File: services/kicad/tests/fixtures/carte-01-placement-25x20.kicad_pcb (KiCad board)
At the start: 2 copper layers, 24.8 x 17 mm, 5 parts, among them J1 IN

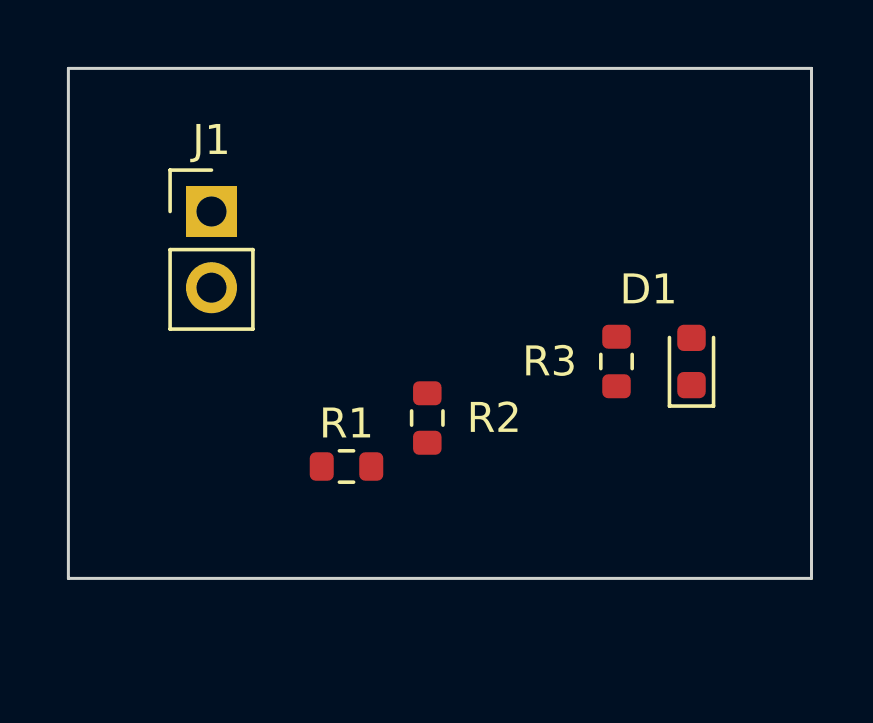
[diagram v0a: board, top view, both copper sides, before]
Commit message: test(banc): contour resserré mesuré sur onze cartes — quatre livrées plus petites (D-2026-09-13-c A) (#179)
* test(banc): les onze cartes en taille heuristique — le validateur applique le contour resserré (A)

Les dimensions des `input/schema.json` du banc valaient « imposées » par
défaut ; `board_size_imposed: false` les rend heuristiques, comme un driver
qui choisit la taille sans que la description la donne. Le validateur
transmet `auto_size_board` à `place_auto` (même contrat que la production)
et imprime la taille du contour resserré à chaque tirage.

Co-Authored-By: Claude Fable 5.1 <noreply@anthropic.com>
Claude-Session: https://claude.ai/code/session_01TnMqm4La2CxQHHB5K8aSSV

* test(examples): quatre cartes livrées plus petites — contour resserré mesuré sur le banc (D-2026-09-13-c A)

Banc rejoué en taille heuristique (phase 1 puis phase 2 à placement gelé) :
carte-01 25x20 -> 24,8x17 (84 % de surface), carte-04 60x45 -> 45x44,8
(75 %), carte-06 80x60 -> 65,2x59,8 (81 %), carte-07 110x80 -> 99,5x79,8
(90 %) — toutes 100 % routées, 0 erreur DRC (vérifié en local), rendus 3D
régénérés. Gain nul sur les cartes denses (le génétique remplit la carte) ;
08 et 09 non livrées (dispersion du routage, surface inchangée) ; carte-11
non livrée (carte d'escalade). Tableau complet dans docs/DECISIONS.md.

Co-Authored-By: Claude Fable 5.1 <noreply@anthropic.com>
Claude-Session: https://claude.ai/code/session_01TnMqm4La2CxQHHB5K8aSSV

* test(kicad): fixture figée pour les tests du contour et des ancrages — examples/ bouge à chaque livraison

Les tests lisaient carte-01/expected/placement.kicad_pcb et supposaient 25x20
avec J1 au coin de la grille ; la livraison de cette PR (24,8x17, J1 déplacé)
les cassait en CI (5 échecs). La copie d'avant devient
tests/fixtures/carte-01-placement-25x20.kicad_pcb : un test ne lit pas ses
hypothèses dans un artefact qui change.

Co-Authored-By: Claude Fable 5.1 <noreply@anthropic.com>
Claude-Session: https://claude.ai/code/session_01TnMqm4L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
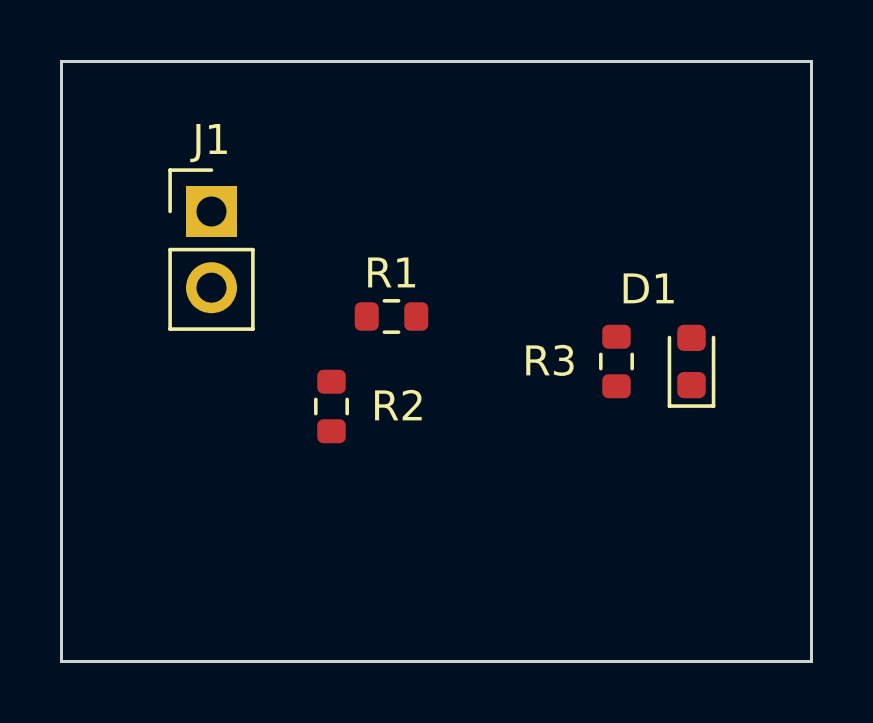
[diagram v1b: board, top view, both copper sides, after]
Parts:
- moved R1 5.22 mm to (147.0, 103.5)
- moved R2 3.22 mm to (145.0, 106.5)
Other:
- board size 24.8 x 17 mm -> 25 x 20 mm
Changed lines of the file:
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@@
 	(title_block
 		(title "Cirqix PCB")
-		(date "2026-09-13")
+		(date "2026-09-12")
 		(rev 1.0)
 		(company "")
@@
 	(net 3 "LED_A")
 	(net 4 "VIN")
+	(gr_rect
+		(start 136 95)
+		(end 161 115)
+		(stroke
+			(width 0.1)
+			(type default)
+		)
+		(fill none)
+		(layer "Edge.Cuts")
+	)
 	(footprint "PinHeader_1x02_P2.54mm_Vertical"
 		(version 20260206)
@@
 		(generator "kicad-footprint-generator")
 		(layer "F.Cu")
-		(at 145.5 108.5 0)
+		(at 147 103.5 0)
 		(descr "Resistor SMD 0603 (1608 Metric), square (rectangular) end terminal, IPC-7351 nominal, (Body size source: IPC-SM-782 page 72, https://www.pcb-3d.com/wordpress/wp-content/uploads/ipc-sm-782a_amendment_1_and_2.pdf)")
 		(tags "resistor")
@@
 		(generator "kicad-footprint-generator")
 		(layer "F.Cu")
-		(at 148.1929 106.8842 270)
+		(at 145 106.5 270)
 		(descr "Resistor SMD 0603 (1608 Metric), square (rectangular) end terminal, IPC-7351 nominal, (Body size source: IPC-SM-782 page 72, https://www.pcb-3d.com/wordpress/wp-content/uploads/ipc-sm-782a_amendment_1_and_2.pdf)")
 		(tags "resistor")
@@
 		)
 	)
-	(gr_rect
-		(start 136.230 95.230)
-		(end 161.000 112.230)
-		(stroke
-			(width 0.1)
-			(type default)
-		)
-		(fill no)
-		(layer "Edge.Cuts")
-	)
 )
